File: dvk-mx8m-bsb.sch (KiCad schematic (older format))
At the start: 14 parts, among them J101 IMX8M-SOM, J102 TEST_1P

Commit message: Add current sense resistors and jumper symbols in the schematic, assign the various signals left unspecified, complete the PWR_EN assignment and verify that thepower sequence would be brought up in the correct order, add an LED to the VBAT_REG rail for debugging purposes (know when the board is receiving power)
Both the GP_LED1 and the HAPTIC motor are able to be controlled via PWM2 by individually MUXing the corresponding pads to PWM2. Only one pin should be MUXed to PWM2 at a time whilst the other is a GPIO, otherwise they will behave identically.

The I2C buses do not need the bus switch found on the EmCraft baseboard since the M.2 modules' power is controlled by PWR_EN and their I2C is level shifted between 1.8V<->3.3V, making it safe to leave them as is.

The various sense resistors have their corresponding parts selected but will be "NC" in the BoM and will not be assembled during manufacturing. To measure the current on the various rails (and WLAN M.2), one will need to break the trace between the two pads and place the corresponding resistor. A jumper (1.27 or 2.45 still needs to be determined) can be used to re-short these pads.

Notes have been added regarding which GPIO pins can easily be interchanged if it improves the layout.

Selected a better/cheaper RJ45 receptacle. Also picked out a well-suited green LED to be used in various spots throughout the board.
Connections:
- net IMU_INT: now also J101.C58 (Pin_58)
- net MIC_SEL: now also J101.D16 (Pin_16)
- net PROX_~INT: now also J101.C35 (Pin_35)
- net HAPTIC: now reaches J101.D5 (Pin_5)
- no-connect marks 79 -> 71
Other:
- note added: "Alternate Functions:"
- note added: "GPIO that can be swapped around:\nGPIO3_IO20\nGPIO3_IO25\nGPIO3_IO19 (was LED1)\nGPIO5_IO05 (was PWM1)\nGPIO5_IO03 (was PWM3)"
- note added: "GPIO3_IO19 (was LED1)"
- note added: "GPIO3_IO20"
- note added: "GPIO3_IO25"
- note added: "GPIO5_IO05 (was PWM1)"
- note added: "Spare GPIO:\nGPIO5_IO03 (was PWM3)"
- note removed: "SAI1_RXD1(GPIO4_IO03)"
- note removed: "SAI1_TXD3(GPIO4_IO15)"
- note removed: "SAI1_TXD6(GPIO4_IO18)"
- note removed: "SAI5_RXC(GPIO3_IO20)"
- note removed: "TODO!!!"
- note removed: "used to be:"
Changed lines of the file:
@@
 Sheet 1 21
 Title "DVK-MX8M-BSB"
-Date "2018-05-16"
+Date "2018-05-18"
 Rev "v0.1.0"
 Comp "Purism SPC"
@@
 	1    0    0    -1
 $EndComp
-Text Notes 3350 12150 0    60   ~ 0
-SAI1_TXD3(GPIO4_IO15)
-Text Notes 3350 12250 0    60   ~ 0
-SAI1_TXD6(GPIO4_IO18)
-Text Notes 3350 12750 0    60   ~ 0
-SAI1_RXD1(GPIO4_IO03)
-Text Notes 3350 12050 0    60   ~ 0
-used to be:
 Text Label 3200 12150 2    60   ~ 0
 BTN1
@@
 Text Notes 3250 3650 0    60   ~ 0
 CAPTOUCH_~RST
-Text Notes 8850 2150 0    60   ~ 0
-TODO!!!
 $Comp
 L 3V3_OUT #PWR015
@@
 NoConn ~ 18600 9450
 NoConn ~ 18600 9650
-NoConn ~ 18600 9850
 NoConn ~ 18600 10050
 NoConn ~ 18600 10850
@@
 NoConn ~ 17900 9550
 NoConn ~ 17900 9250
-NoConn ~ 17900 9350
 NoConn ~ 18600 5250
-NoConn ~ 18600 5450
 NoConn ~ 18600 6050
 NoConn ~ 17900 4050
 NoConn ~ 17900 4150
 NoConn ~ 17900 4250
-NoConn ~ 17900 4350
 NoConn ~ 17900 4450
 NoConn ~ 17900 3550
@@
 	18500 5250 18600 5250
 Wire Wire Line
-	18500 5450 18600 5450
+	18500 5450 19650 5450
 Wire Wire Line
 	18500 5650 19650 5650
@@
 	18000 4250 17900 4250
 Wire Wire Line
-	18000 4350 17900 4350
+	18000 4350 16850 4350
 Wire Wire Line
 	18000 4450 17900 4450
@@
 	18000 9250 17900 9250
 Wire Wire Line
-	18000 9350 17900 9350
+	18000 9350 16850 9350
 Wire Wire Line
 	18500 9450 18600 9450
@@
 	18500 9650 18600 9650
 Wire Wire Line
-	18500 9850 18600 9850
+	18500 9850 19650 9850
 Wire Wire Line
 	18500 10050 18600 10050
@@
 Text Label 7800 2900 2    60   ~ 0
 MIC_SEL
-NoConn ~ 7800 2900
 Text Notes 5150 16000 0    60   ~ 0
 TODO:\nGNSS\nMIPI CSI/DSI
@@
 Text Label 7800 14400 2    60   ~ 0
 IMU_INT
-NoConn ~ 7800 14250
-NoConn ~ 7800 14400
 $Sheet
 S 5150 14700 1400 500
@@
 Wire Wire Line
 	6550 15500 7800 15500
-NoConn ~ 7800 15500
 Text Label 7800 6450 2    60   ~ 0
 SAI5_TX_BCLK
@@
 Text Label 16850 5650 0    60   ~ 0
 SAI5_TXD
-Text Notes 7900 2750 0    60   ~ 0
-SAI5_RXC(GPIO3_IO20)
+Text Notes 7850 2750 0    60   ~ 0
+GPIO3_IO20
 NoConn ~ 3200 11200
 NoConn ~ 3200 11100
@@
 	1    0    0    -1
 $EndComp
+Text Label 16850 9350 0    60   ~ 0
+HAPTIC
+Text Label 7800 15500 2    60   ~ 0
+HAPTIC
+Text Notes 3250 3550 0    60   ~ 12
+Alternate Functions:
+Text Notes 9950 1125 0    60   ~ 0
+Spare GPIO:\nGPIO5_IO03 (was PWM3)
+Text Notes 7850 14250 0    60   ~ 0
+GPIO3_IO19 (was LED1)
+Text Label 16850 4350 0    60   ~ 0
+PROX_~INT
+Text Notes 11200 1500 0    60   ~ 0
+GPIO that can be swapped around:\nGPIO3_IO20\nGPIO3_IO25\nGPIO3_IO19 (was LED1)\nGPIO5_IO05 (was PWM1)\nGPIO5_IO03 (was PWM3)
+Text Notes 7850 14400 0    60   ~ 0
+GPIO3_IO25
+Text Label 19650 5450 2    60   ~ 0
+IMU_INT
+Text Notes 7850 2900 0    60   ~ 0
+GPIO5_IO05 (was PWM1)
+Text Label 19650 9850 2    60   ~ 0
+MIC_SEL
 $EndSCHEMATC

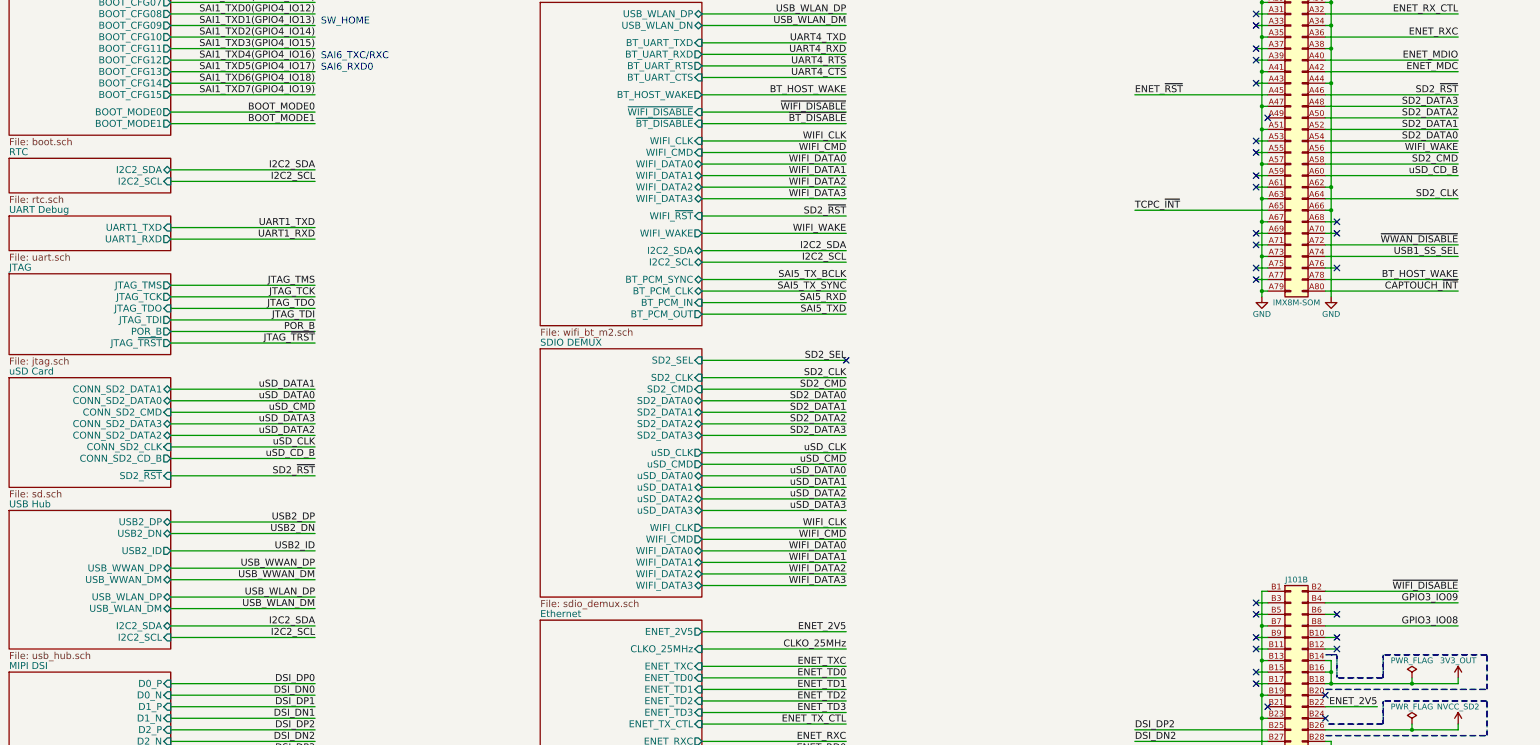
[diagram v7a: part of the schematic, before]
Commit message: Added schematic page with USB hub/SD Card controller USB2660 deleted old USB hub and SDIO demultiplexer
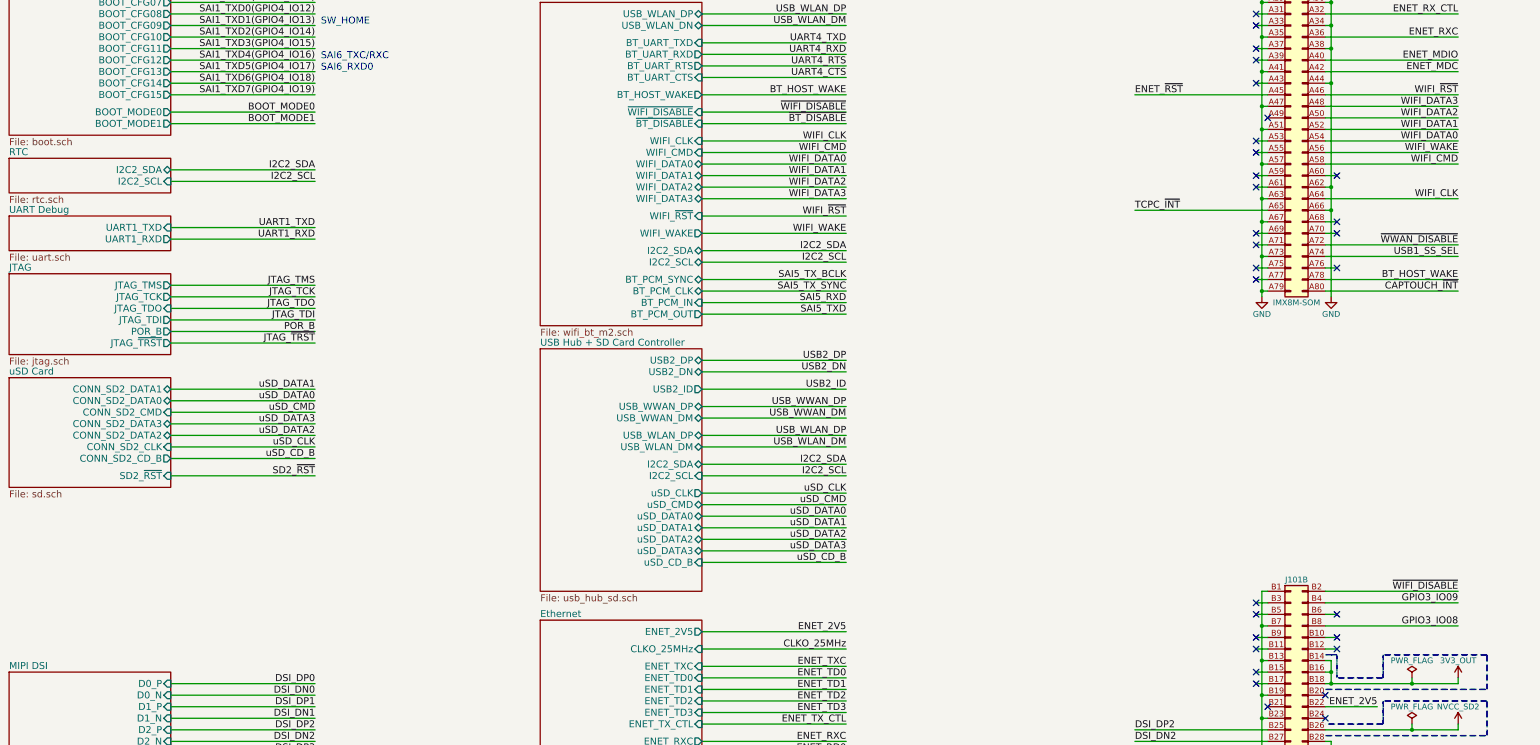
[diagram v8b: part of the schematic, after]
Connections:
- net SD2_CLK is gone; now on net WIFI_CLK: J101.A64 (Pin_64)
- net SD2_CMD is gone; now on net WIFI_CMD: J101.A58 (Pin_58)
- net SD2_DATA0 is gone; now on net WIFI_DATA0: J101.A54 (Pin_54)
- net SD2_DATA1 is gone; now on net WIFI_DATA1: J101.A52 (Pin_52)
- net SD2_DATA2 is gone; now on net WIFI_DATA2: J101.A50 (Pin_50)
- net SD2_DATA3 is gone; now on net WIFI_DATA3: J101.A48 (Pin_48)
- net SD2_~RST: no longer J101.A46 (Pin_46)
- net uSD_CD_B: no longer J101.A60 (Pin_60)
- new net WIFI_~RST: J101.A46 (Pin_46)
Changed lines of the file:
@@
 $Descr A2 23386 16535
 encoding utf-8
-Sheet 1 21
+Sheet 1 20
 Title "DVK-MX8M-BSB"
 Date "2018-05-18"
@@
 $EndSheet
 $Sheet
-S 550  8450 1400 1200
+S 5150 7050 1400 2100
 U 5ADF72D2
-F0 "USB Hub" 60
-F1 "usb_hub.sch" 60
-F2 "USB2_DN" B R 1950 8650 60
-F3 "USB2_DP" B R 1950 8550 60
-F4 "I2C2_SCL" I R 1950 9550 60
-F5 "I2C2_SDA" B R 1950 9450 60
-F6 "USB2_ID" O R 1950 8800 60
-F7 "USB_WWAN_DP" B R 1950 8950 60
-F8 "USB_WWAN_DM" B R 1950 9050 60
-F9 "USB_WLAN_DP" B R 1950 9200 60
-F10 "USB_WLAN_DM" B R 1950 9300 60
+F0 "USB Hub + SD Card Controller" 60
+F1 "usb_hub_sd.sch" 60
+F2 "USB2_DN" B R 6550 7250 60
+F3 "USB2_DP" B R 6550 7150 60
+F4 "I2C2_SCL" I R 6550 8150 60
+F5 "I2C2_SDA" B R 6550 8050 60
+F6 "USB2_ID" O R 6550 7400 60
+F7 "USB_WWAN_DP" B R 6550 7550 60
+F8 "USB_WWAN_DM" B R 6550 7650 60
+F9 "USB_WLAN_DP" B R 6550 7800 60
+F10 "USB_WLAN_DM" B R 6550 7900 60
+F11 "uSD_CLK" O R 6550 8300 60
+F12 "uSD_CMD" B R 6550 8400 60
+F13 "uSD_DATA0" B R 6550 8500 60
+F14 "uSD_DATA1" B R 6550 8600 60
+F15 "uSD_DATA2" B R 6550 8700 60
+F16 "uSD_DATA3" B R 6550 8800 60
+F17 "uSD_CD_B" I R 6550 8900 60
 $EndSheet
 $Sheet
@@
 Text Label 3200 8150 2    60   ~ 0
 SD2_~RST
-Text Label 13100 4850 2    60   ~ 0
-SD2_~RST
 Text Label 3200 12750 2    60   ~ 0
 GPIO1_IO13
@@
 uSD_CLK
 Text Label 3200 8000 2    60   ~ 0
-uSD_CD_B
-Text Label 13100 5150 2    60   ~ 0
-SD2_DATA1
-Text Label 13100 5250 2    60   ~ 0
-SD2_DATA0
-Text Label 13100 5450 2    60   ~ 0
-SD2_CMD
-Text Label 13100 4950 2    60   ~ 0
-SD2_DATA3
-Text Label 13100 5050 2    60   ~ 0
-SD2_DATA2
-Text Label 13100 5750 2    60   ~ 0
-SD2_CLK
-Text Label 13100 5550 2    60   ~ 0
 uSD_CD_B
 Text Label 16850 11350 0    60   ~ 0
@@
 Text Label 19650 11950 2    60   ~ 0
 USB2_DP
-Text Label 3200 8550 2    60   ~ 0
+Text Label 7800 7150 2    60   ~ 0
 USB2_DP
-Text Label 3200 8650 2    60   ~ 0
+Text Label 7800 7250 2    60   ~ 0
 USB2_DN
-Text Label 3200 9450 2    60   ~ 0
+Text Label 7800 8050 2    60   ~ 0
 I2C2_SDA
-Text Label 3200 9550 2    60   ~ 0
+Text Label 7800 8150 2    60   ~ 0
 I2C2_SCL
 Text Label 16850 12850 0    60   ~ 0
@@
 Text Label 16850 12750 0    60   ~ 0
 USB2_VBUS
-Text Label 3200 8800 2    60   ~ 0
+Text Label 7800 7400 2    60   ~ 0
 USB2_ID
-Text Label 3200 8950 2    60   ~ 0
+Text Label 7800 7550 2    60   ~ 0
 USB_WWAN_DP
-Text Label 3200 9050 2    60   ~ 0
+Text Label 7800 7650 2    60   ~ 0
 USB_WWAN_DM
-Text Label 3200 9300 2    60   ~ 0
+Text Label 7800 7900 2    60   ~ 0
 USB_WLAN_DM
 Text Label 3200 13850 2    60   ~ 0
@@
 Text Label 7800 5000 2    60   ~ 0
 ~WIFI_DISABLE
-Text Label 3200 9200 2    60   ~ 0
+Text Label 7800 7800 2    60   ~ 0
 USB_WLAN_DP
 NoConn ~ 11350 9250
@@
 NoConn ~ 12050 6050
 NoConn ~ 12050 6350
-Text Label 7800 7600 2    60   ~ 0
-SD2_DATA1
-Text Label 7800 7500 2    60   ~ 0
-SD2_DATA0
-Text Label 7800 7400 2    60   ~ 0
-SD2_CMD
-Text Label 7800 7800 2    60   ~ 0
-SD2_DATA3
-Text Label 7800 7700 2    60   ~ 0
-SD2_DATA2
-Text Label 7800 7300 2    60   ~ 0
-SD2_CLK
-Text Label 7800 7150 2    60   ~ 0
-SD2_SEL
-Text Label 7800 8250 2    60   ~ 0
-uSD_DATA1
-Text Label 7800 8150 2    60   ~ 0
-uSD_DATA0
-Text Label 7800 8050 2    60   ~ 0
-uSD_CMD
-Text Label 7800 8450 2    60   ~ 0
-uSD_DATA3
-Text Label 7800 8350 2    60   ~ 0
-uSD_DATA2
-Text Label 7800 7950 2    60   ~ 0
-uSD_CLK
-Text Label 7800 8900 2    60   ~ 0
+Text Label 13100 5150 2    60   ~ 0
 WIFI_DATA1
-Text Label 7800 8800 2    60   ~ 0
+Text Label 13100 5250 2    60   ~ 0
 WIFI_DATA0
-Text Label 7800 8700 2    60   ~ 0
+Text Label 13100 5450 2    60   ~ 0
 WIFI_CMD
-Text Label 7800 9100 2    60   ~ 0
+Text Label 13100 4950 2    60   ~ 0
 WIFI_DATA3
-Text Label 7800 9000 2    60   ~ 0
+Text Label 13100 5050 2    60   ~ 0
 WIFI_DATA2
-Text Label 7800 8600 2    60   ~ 0
+Text Label 13100 5750 2    60   ~ 0
 WIFI_CLK
 Text Label 7800 5550 2    60   ~ 0
@@
 Text Label 7800 5250 2    60   ~ 0
 WIFI_CLK
-NoConn ~ 7800 7150
-$Sheet
-S 5150 7050 1400 2150
-U 5AEA7739
-F0 "SDIO DEMUX" 60
-F1 "sdio_demux.sch" 60
-F2 "SD2_SEL" I R 6550 7150 60
-F3 "SD2_CLK" I R 6550 7300 60
-F4 "SD2_CMD" I R 6550 7400 60
-F5 "SD2_DATA0" B R 6550 7500 60
-F6 "SD2_DATA1" B R 6550 7600 60
-F7 "SD2_DATA2" B R 6550 7700 60
-F8 "SD2_DATA3" B R 6550 7800 60
-F9 "uSD_CLK" O R 6550 7950 60
-F10 "uSD_CMD" O R 6550 8050 60
-F11 "uSD_DATA0" B R 6550 8150 60
-F12 "uSD_DATA1" B R 6550 8250 60
-F13 "uSD_DATA2" B R 6550 8350 60
-F14 "uSD_DATA3" B R 6550 8450 60
-F15 "WIFI_CLK" O R 6550 8600 60
-F16 "WIFI_CMD" O R 6550 8700 60
-F17 "WIFI_DATA0" B R 6550 8800 60
-F18 "WIFI_DATA1" B R 6550 8900 60
-F19 "WIFI_DATA2" B R 6550 9000 60
-F20 "WIFI_DATA3" B R 6550 9100 60
-$EndSheet
 Text Label 7800 5900 2    60   ~ 0
-SD2_~RST
+WIFI_~RST
 Text Label 7800 6200 2    60   ~ 0
 I2C2_SDA
@@
 	1950 8000 3200 8000
 Wire Wire Line
-	11950 5150 13100 5150
-Wire Wire Line
-	11950 5250 13100 5250
-Wire Wire Line
-	11950 5450 13100 5450
-Wire Wire Line
-	11950 4950 13100 4950
-Wire Wire Line
-	11950 5050 13100 5050
-Wire Wire Line
-	11950 5750 13100 5750
-Wire Wire Line
-	11950 5550 13100 5550
-Wire Wire Line
 	18000 11350 16850 11350
 Wire Wire Line
@@
 	18500 11950 19650 11950
 Wire Wire Line
-	1950 8550 3200 8550
-Wire Wire Line
-	1950 8650 3200 8650
-Wire Wire Line
-	1950 9450 3200 9450
-Wire Wire Line
-	1950 9550 3200 9550
+	6550 7150 7800 7150
+Wire Wire Line
+	6550 7250 7800 7250
+Wire Wire Line
+	6550 8050 7800 8050
+Wire Wire Line
+	6550 8150 7800 8150
 Wire Wire Line
 	18000 12750 16700 12750
@@
 	18000 12850 16850 12850
 Wire Wire Line
-	1950 8800 3200 8800
-Wire Wire Line
-	1950 8950 3200 8950
-Wire Wire Line
-	1950 9050 3200 9050
-Wire Wire Line
-	1950 9200 3200 9200
-Wire Wire Line
-	1950 9300 3200 9300
+	6550 7400 7800 7400
+Wire Wire Line
+	6550 7550 7800 7550
+Wire Wire Line
+	6550 7650 7800 7650
+Wire Wire Line
+	6550 7800 7800 7800
+Wire Wire Line
+	6550 7900 7800 7900
 Wire Wire Line
 	1950 13850 3200 13850
@@
 	18000 11750 16850 11750
 Wire Wire Line
-	6550 7300 7800 7300
-Wire Wire Line
-	6550 7400 7800 7400
-Wire Wire Line
-	6550 7500 7800 7500
-Wire Wire Line
-	6550 7600 7800 7600
-Wire Wire Line
-	6550 7700 7800 7700
-Wire Wire Line
-	6550 7800 7800 7800
-Wire Wire Line
-	6550 7150 7800 7150
-Wire Wire Line
-	6550 7950 7800 7950
-Wire Wire Line
-	6550 8050 7800 8050
-Wire Wire Line
-	6550 8150 7800 8150
-Wire Wire Line
-	6550 8250 7800 8250
-Wire Wire Line
-	6550 8350 7800 8350
-Wire Wire Line
-	6550 8450 7800 8450
-Wire Wire Line
-	6550 8600 7800 8600
-Wire Wire Line
-	6550 8700 7800 8700
-Wire Wire Line
-	6550 8800 7800 8800
-Wire Wire Line
-	6550 8900 7800 8900
-Wire Wire Line
-	6550 9000 7800 9000
-Wire Wire Line
-	6550 9100 7800 9100
+	11950 5750 13100 5750
+Wire Wire Line
+	11950 5450 13100 5450
+Wire Wire Line
+	11950 5250 13100 5250
+Wire Wire Line
+	11950 5150 13100 5150
+Wire Wire Line
+	11950 5050 13100 5050
+Wire Wire Line
+	11950 4950 13100 4950
 Wire Wire Line
 	6550 5250 7800 5250
@@
 Text Label 19650 9850 2    60   ~ 0
 MIC_SEL
+Text Label 7800 8600 2    60   ~ 0
+uSD_DATA1
+Text Label 7800 8500 2    60   ~ 0
+uSD_DATA0
+Text Label 7800 8400 2    60   ~ 0
+uSD_CMD
+Text Label 7800 8800 2    60   ~ 0
+uSD_DATA3
+Text Label 7800 8700 2    60   ~ 0
+uSD_DATA2
+Text Label 7800 8300 2    60   ~ 0
+uSD_CLK
+Text Label 7800 8900 2    60   ~ 0
+uSD_CD_B
+Wire Wire Line
+	6550 8600 7800 8600
+Wire Wire Line
+	6550 8500 7800 8500
+Wire Wire Line
+	6550 8400 7800 8400
+Wire Wire Line
+	6550 8800 7800 8800
+Wire Wire Line
+	6550 8700 7800 8700
+Wire Wire Line
+	6550 8300 7800 8300
+Wire Wire Line
+	6550 8900 7800 8900
+Text Label 13100 4850 2    60   ~ 0
+WIFI_~RST
+Wire Wire Line
+	11950 5550 12050 5550
+NoConn ~ 12050 5550
 $EndSCHEMATC
